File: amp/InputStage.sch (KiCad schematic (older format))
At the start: 20 parts

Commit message: started vac layout
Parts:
- removed U? (x3): TL074, symbol Amplifier_Operational:TL074
- J1, J10, J2, J3, J4, J7, J8, J9: renamed from J?; footprint (none) -> synth:3.5MM_Jack_Breakout_Vertical
- J5: renamed from J?; footprint (none) -> KiCad/kicad-footprints/Connector_PinHeader_2.54mm.pretty:PinHeader_2x04_P2.54mm_Vertical
- U1: renamed from U?; footprint (none) -> KiCad/Housings_DIP.pretty:DIP-14_W7.62mm
- gave numbers to parts that had none: 3
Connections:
- net AIN_DEFAULT is gone; now on net A_IN_DEFAULT: J1.TN, J5.1 (Pin_1)
- net BIN_DEFAULT is gone; now on net B_IN_DEFAULT: J2.TN, J5.2 (Pin_2)
- net CIN_DEFAULT is gone; now on net C_IN_DEFAULT: J3.TN, J5.3 (Pin_3)
- net DIN_DEFAULT is gone; now on net D_IN_DEFAULT: J4.TN, J5.4 (Pin_4)
- net A_CV: now also U1.5 (+); no longer U1.3 (+)
- net B_CV: now also U1.10 (+); no longer U1.3 (+)
- net B_CV_DEFAULT: now also U1.6 (-), U1.7; no longer U1.1, U1.2 (-)
- net C_CV: now also U1.12 (+); no longer U1.3 (+)
- net C_CV_DEFAULT: now also U1.8, U1.9 (-); no longer U1.1, U1.2 (-)
- net D_CV_DEFAULT: now also U1.13 (-), U1.14; no longer U1.1, U1.2 (-)
- net D_IN_DEFAULT: now reaches J5.5 (Pin_5)
- net C_IN_DEFAULT: now reaches J5.6 (Pin_6)
- net B_IN_DEFAULT: now reaches J5.7 (Pin_7)
- net A_IN_DEFAULT: now reaches J5.8 (Pin_8)
- net AIN renamed A_IN
- net BIN renamed B_IN
- net CIN renamed C_IN
- net DIN renamed D_IN
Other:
- moved on the sheet: U1E, U2E, U3E

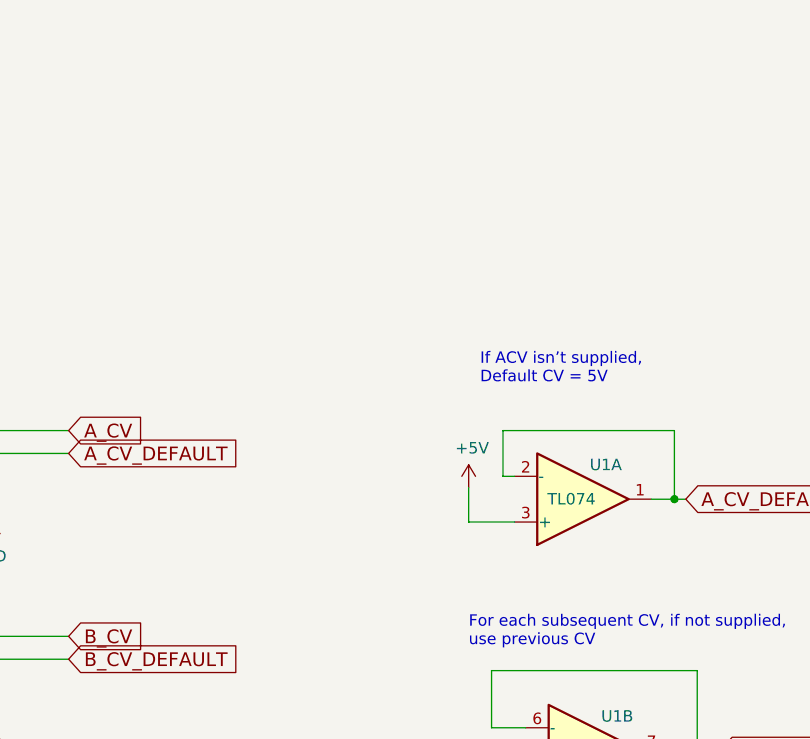
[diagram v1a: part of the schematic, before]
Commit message: update components
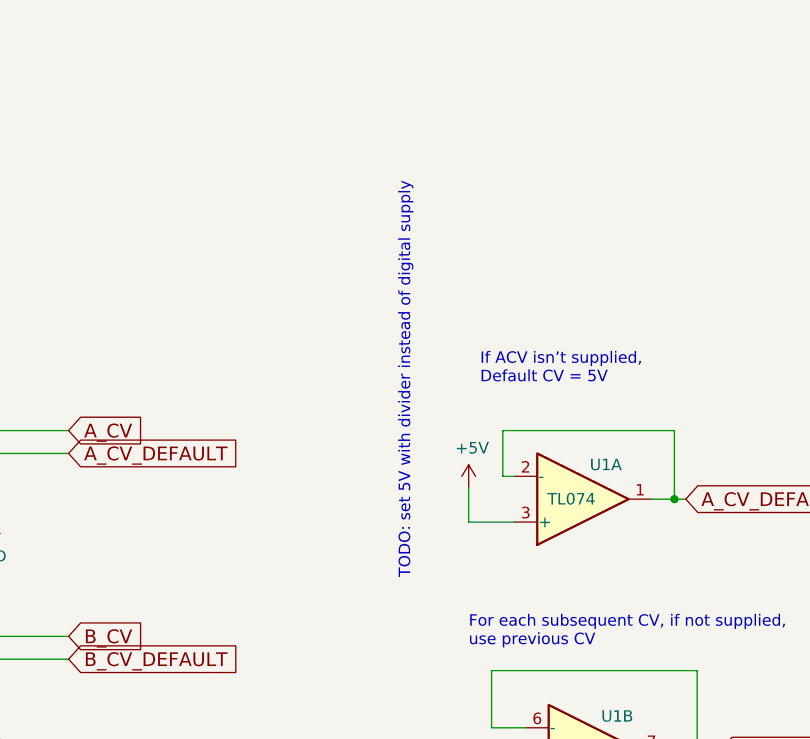
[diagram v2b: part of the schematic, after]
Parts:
- J5: footprint KiCad/kicad-footprints/Connector_PinHeader_2.54mm.pretty:PinHeader_2x04_P2.54mm_Vertical -> Connector_PinHeader_2.54mm:PinHeader_2x04_P2.54mm_Vertical
- U1: footprint KiCad/Housings_DIP.pretty:DIP-14_W7.62mm -> Package_DIP:DIP-14_W7.62mm
- U2, U3: footprint KiCad/Housings_DIP.pretty:DIP-16_W7.62mm -> Package_DIP:DIP-16_W7.62mm
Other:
- note added: "TODO: set 5V with divider instead of digital supply"
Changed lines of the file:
@@
 F 0 "U2" H 10308 1196 50  0000 L CNN
 F 1 "LM13700" H 10308 1105 50  0000 L CNN
-F 2 "KiCad/Housings_DIP.pretty:DIP-16_W7.62mm" H 10050 1175 50  0001 C CNN
+F 2 "Package_DIP:DIP-16_W7.62mm" H 10050 1175 50  0001 C CNN
 F 3 "http://www.ti.com/lit/ds/symlink/lm13700.pdf" H 10050 1175 50  0001 C CNN
 	5    10350 1150
@@
 F 0 "U1" H 6600 1150 50  0000 C CNN
 F 1 "TL074" H 6450 1300 50  0000 C CNN
-F 2 "KiCad/Housings_DIP.pretty:DIP-14_W7.62mm" H 6450 1400 50  0001 C CNN
+F 2 "Package_DIP:DIP-14_W7.62mm" H 6450 1400 50  0001 C CNN
 F 3 "http://www.ti.com/lit/ds/symlink/tl071.pdf" H 6550 1500 50  0001 C CNN
 	1    6500 1300
@@
 F 0 "U1" H 9858 1196 50  0000 L CNN
 F 1 "TL074" H 9858 1105 50  0000 L CNN
-F 2 "KiCad/Housings_DIP.pretty:DIP-14_W7.62mm" H 9850 1250 50  0001 C CNN
+F 2 "Package_DIP:DIP-14_W7.62mm" H 9850 1250 50  0001 C CNN
 F 3 "http://www.ti.com/lit/ds/symlink/tl071.pdf" H 9950 1350 50  0001 C CNN
 	5    9900 1150
@@
 F 0 "U1" H 6650 2250 50  0000 C CNN
 F 1 "TL074" H 6500 2400 50  0000 C CNN
-F 2 "KiCad/Housings_DIP.pretty:DIP-14_W7.62mm" H 6500 2500 50  0001 C CNN
+F 2 "Package_DIP:DIP-14_W7.62mm" H 6500 2500 50  0001 C CNN
 F 3 "http://www.ti.com/lit/ds/symlink/tl071.pdf" H 6600 2600 50  0001 C CNN
 	2    6550 2400
@@
 F 0 "U1" H 6650 2900 50  0000 C CNN
 F 1 "TL074" H 6500 3050 50  0000 C CNN
-F 2 "KiCad/Housings_DIP.pretty:DIP-14_W7.62mm" H 6500 3150 50  0001 C CNN
+F 2 "Package_DIP:DIP-14_W7.62mm" H 6500 3150 50  0001 C CNN
 F 3 "http://www.ti.com/lit/ds/symlink/tl071.pdf" H 6600 3250 50  0001 C CNN
 	3    6550 3050
@@
 F 0 "U1" H 6650 3550 50  0000 C CNN
 F 1 "TL074" H 6500 3700 50  0000 C CNN
-F 2 "KiCad/Housings_DIP.pretty:DIP-14_W7.62mm" H 6500 3800 50  0001 C CNN
+F 2 "Package_DIP:DIP-14_W7.62mm" H 6500 3800 50  0001 C CNN
 F 3 "http://www.ti.com/lit/ds/symlink/tl071.pdf" H 6600 3900 50  0001 C CNN
 	4    6550 3700
@@
 F 0 "U3" H 10858 1196 50  0000 L CNN
 F 1 "LM13700" H 10858 1105 50  0000 L CNN
-F 2 "KiCad/Housings_DIP.pretty:DIP-16_W7.62mm" H 10600 1175 50  0001 C CNN
+F 2 "Package_DIP:DIP-16_W7.62mm" H 10600 1175 50  0001 C CNN
 F 3 "http://www.ti.com/lit/ds/symlink/lm13700.pdf" H 10600 1175 50  0001 C CNN
 	5    10900 1150
@@
 F 0 "J5" H 1800 5667 50  0000 C CNN
 F 1 "Conn_02x04_Counter_Clockwise" H 1800 5576 50  0000 C CNN
-F 2 "KiCad/kicad-footprints/Connector_PinHeader_2.54mm.pretty:PinHeader_2x04_P2.54mm_Vertical" H 1750 5350 50  0001 C CNN
+F 2 "Connector_PinHeader_2.54mm:PinHeader_2x04_P2.54mm_Vertical" H 1750 5350 50  0001 C CNN
 F 3 "~" H 1750 5350 50  0001 C CNN
 	1    1750 5350
@@
 Wire Wire Line
 	9800 700  9800 850
+Text Notes 5750 1650 1    50   ~ 0
+TODO: set 5V with divider instead of digital supply
 $EndSCHEMATC

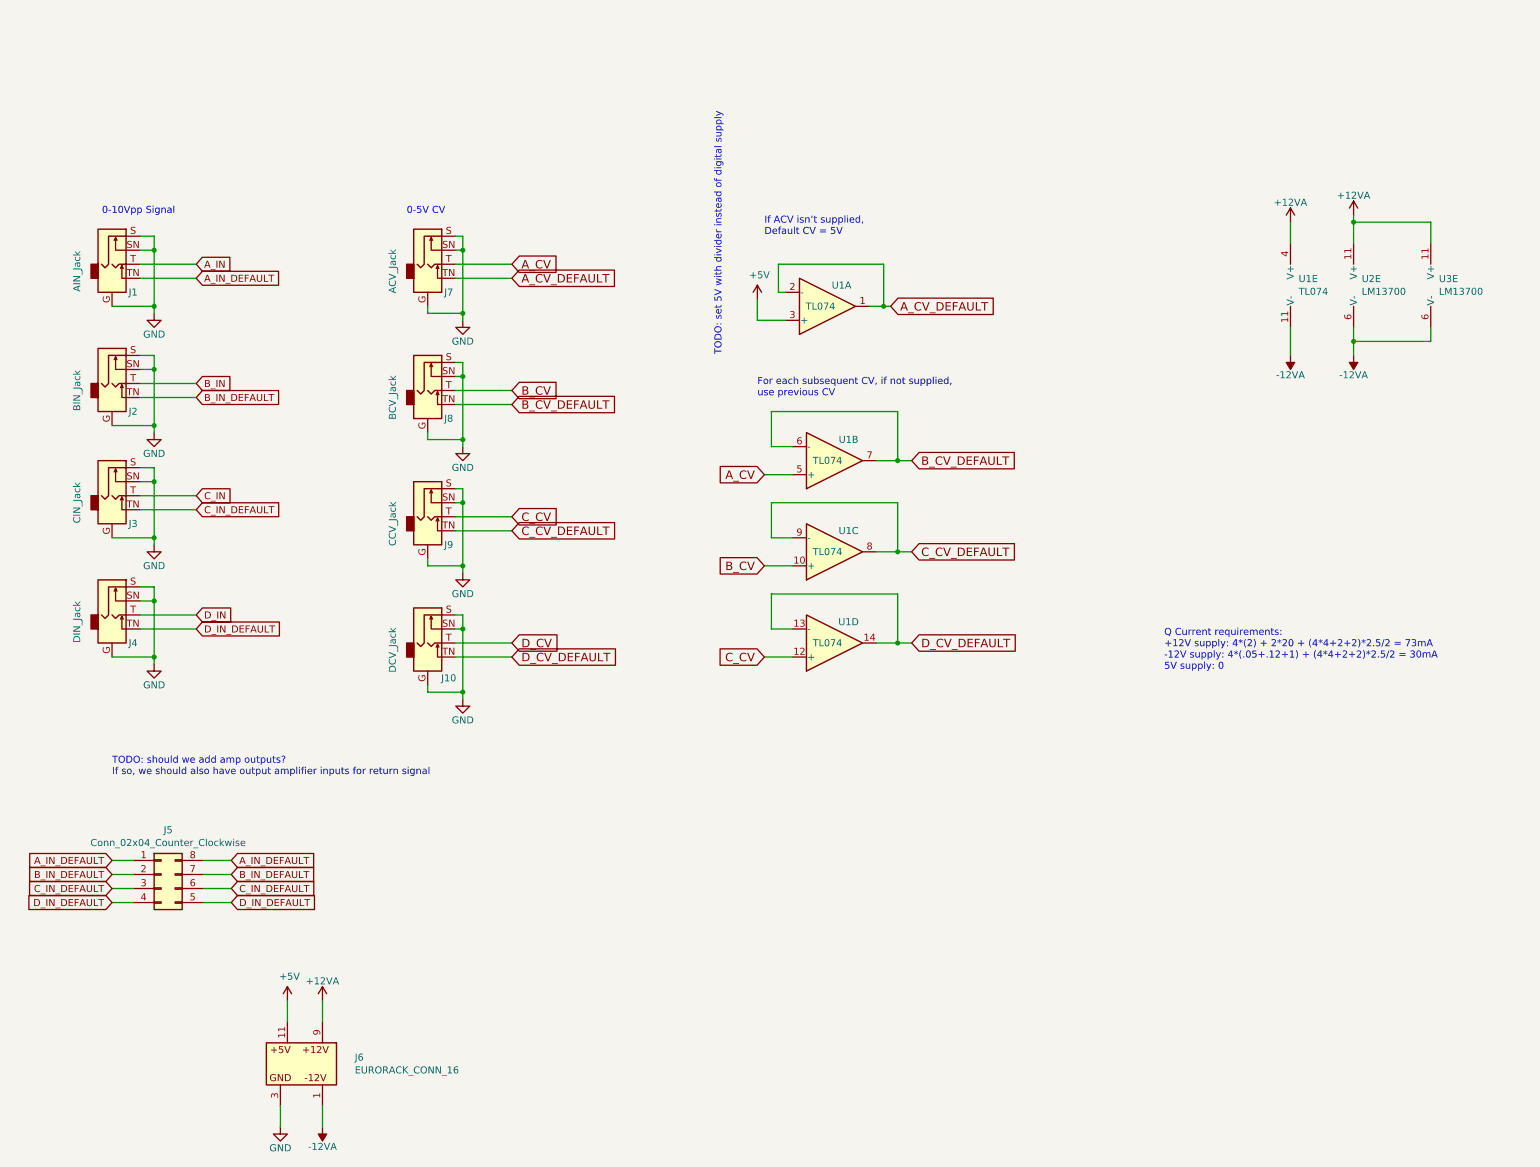
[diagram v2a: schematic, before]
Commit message: get rid of propigating controls
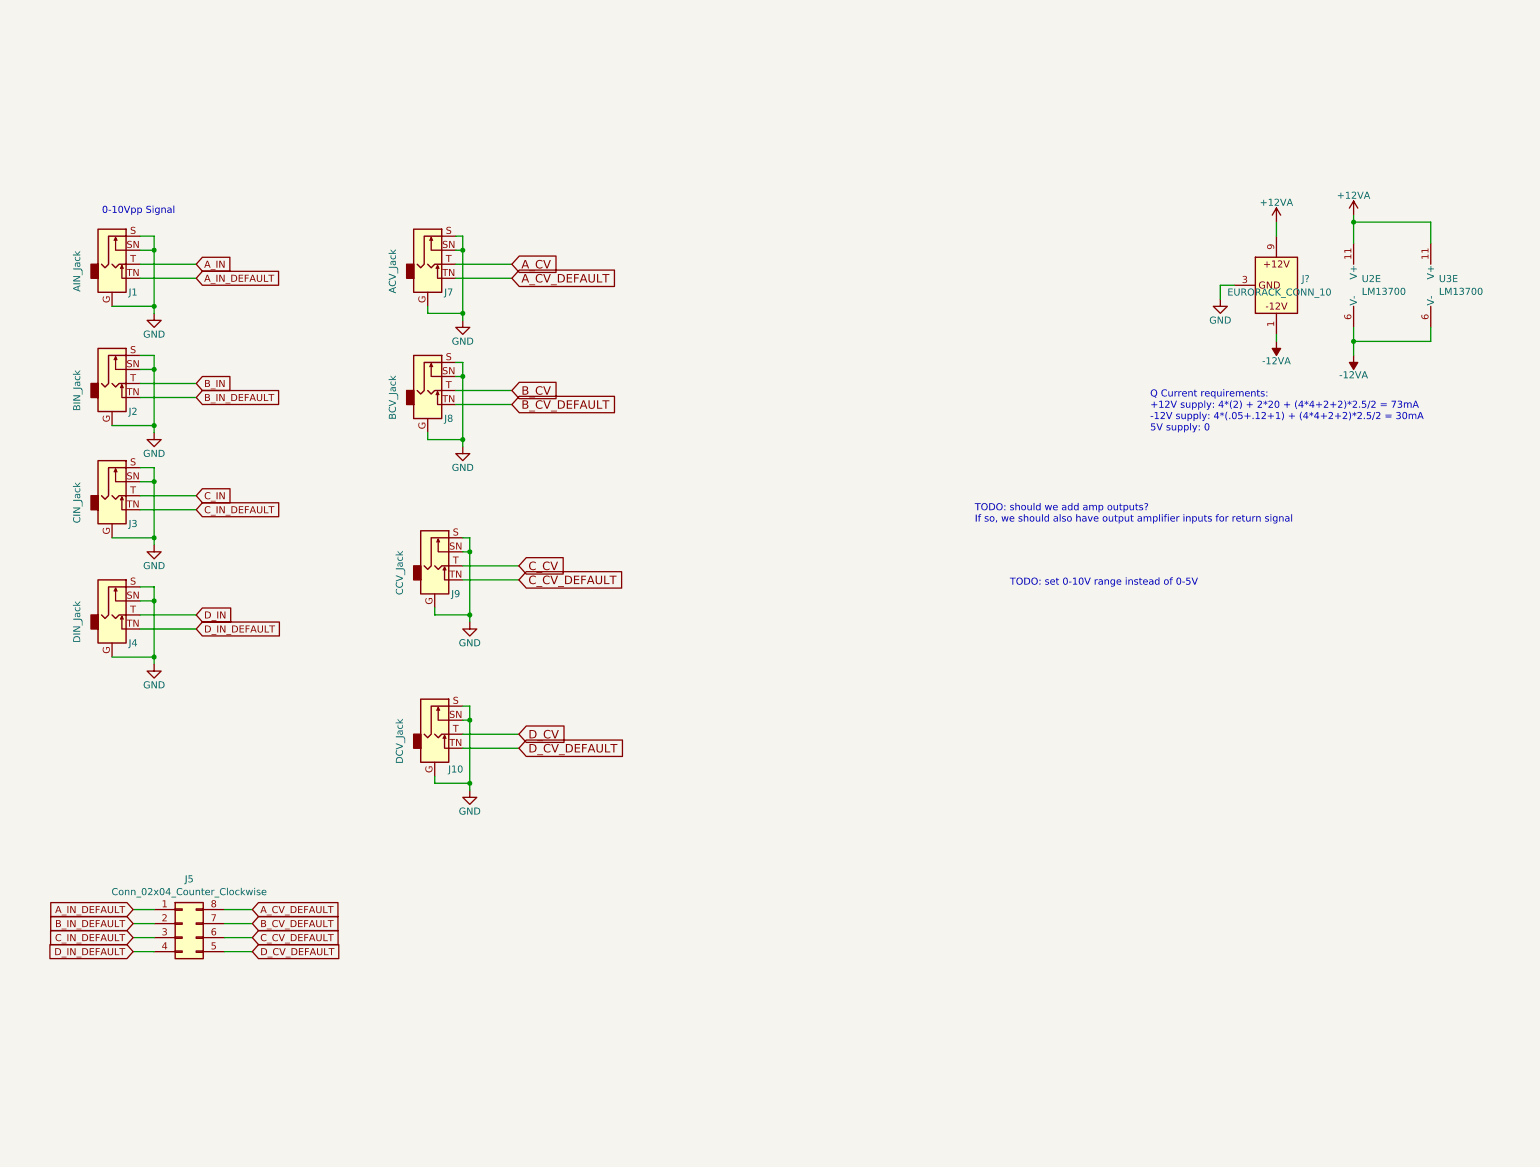
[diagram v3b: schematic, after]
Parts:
- removed J6: EURORACK_CONN_16, synth:EURORACK_16_IDC, symbol synth:EURORACK_CONN_16
- removed U1: TL074, Package_DIP:DIP-14_W7.62mm, symbol Amplifier_Operational:TL074
- added J?: EURORACK_CONN_10, synth:EURORACK_10_IDC, symbol synth:EURORACK_CONN_10
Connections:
- net +12VA: now also J?.9 (12V_P)
- net -12VA: now also J?.1 (12V_N)
- net A_CV_DEFAULT: now also J5.8 (Pin_8)
- net A_IN_DEFAULT: no longer J5.8 (Pin_8)
- net B_CV_DEFAULT: now also J5.7 (Pin_7)
- net B_IN_DEFAULT: no longer J5.7 (Pin_7)
- net C_CV_DEFAULT: now also J5.6 (Pin_6)
- net C_IN_DEFAULT: no longer J5.6 (Pin_6)
- net D_CV_DEFAULT: now also J5.5 (Pin_5)
- net D_IN_DEFAULT: no longer J5.5 (Pin_5)
- net GND: now also J?.3 (GND)
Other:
- note added: "TODO: set 0-10V range instead of 0-5V"
- note removed: "0-5V CV"
- note removed: "For each subsequent CV, if not supplied,\nuse previous CV"
- note removed: "If ACV isn’t supplied,\nDefault CV = 5V"
- note removed: "TODO: set 5V with divider instead of digital supply"
- moved on the sheet: J10, J5, J9

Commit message: adjusted amp to a 10V control voltage range
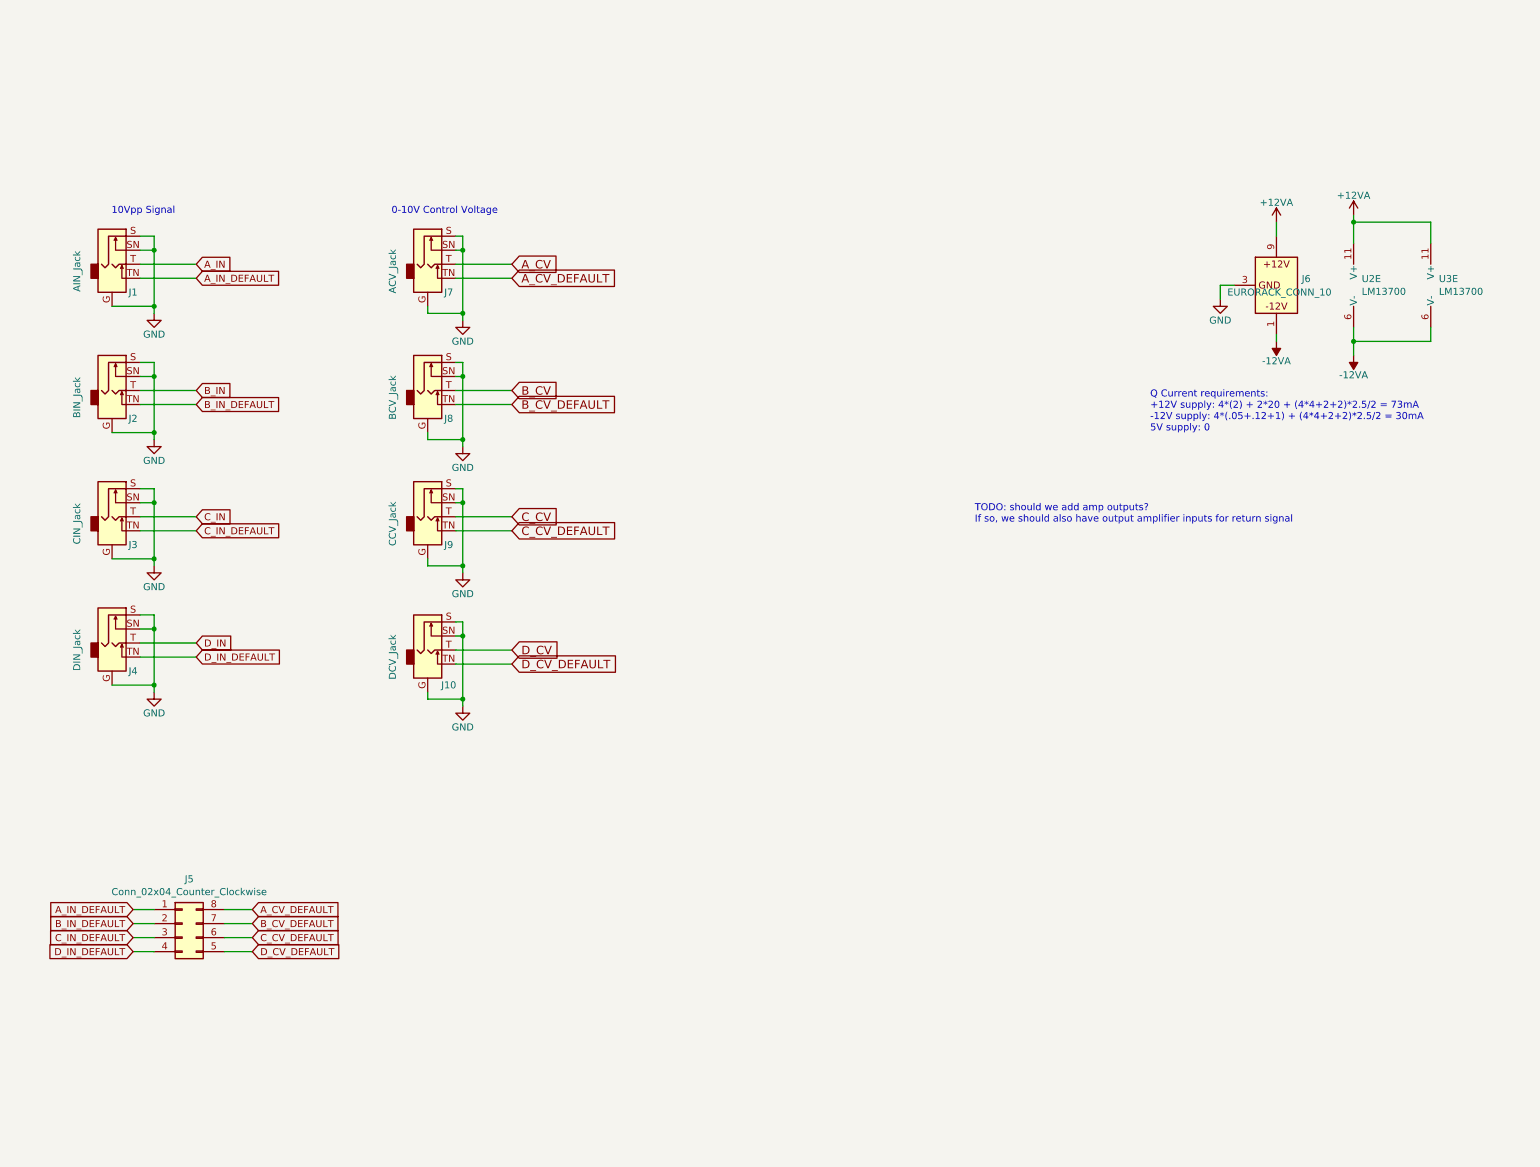
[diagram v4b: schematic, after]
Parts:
- gave numbers to parts that had none: 1
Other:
- note added: "0-10V Control Voltage"
- note added: "10Vpp Signal"
- note removed: "0-10Vpp Signal"
- note removed: "TODO: set 0-10V range instead of 0-5V"
- moved on the sheet: J10, J2, J3, J4, J9
